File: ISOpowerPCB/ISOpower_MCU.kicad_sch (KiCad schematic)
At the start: 28 parts, among them J2 Conn_01x05_Male, J3 Conn_01x04_Male, J4 Conn_01x06_Male, J5 Conn_01x10_Male, J6 PCB_PIN_header_male, J7 i2c Header, J8 AVR-ISP-6, SW1 SW_Push, U1 ESP32-WROOM-32, U2 IFX27001TFV33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

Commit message: adding logic for fault indication
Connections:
- net GND1 is gone; now on net GND: L1.2
- net GND: now also U1.15 (GND), U1.38 (GND), U1.39 (GND)
- no-connect marks 0 -> 3
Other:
- note added: "This needs to be held high at a minimum"
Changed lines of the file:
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@@
   (junction (at 204.47 85.09) (diameter 0) (color 0 0 0 0)
   )
+  (junction (at 54.61 182.88) (diameter 0) (color 0 0 0 0)
+  )
+  (junction (at 57.15 182.88) (diameter 0) (color 0 0 0 0)
+  )
   (junction (at 49.53 35.56) (diameter 0) (color 0 0 0 0)
   )
@@
   (junction (at 129.54 172.72) (diameter 0) (color 0 0 0 0)
   )
+  (no_connect (at 154.94 63.5))
+  (no_connect (at 199.39 80.01))
+  (no_connect (at 209.55 80.01))
   (wire (pts (xy 185.42 106.68) (xy 254 106.68))
     (stroke (width 0) (type default) (color 0 0 0 0))
@@
     (stroke (width 0) (type default) (color 0 0 0 0))
   )
+  (wire (pts (xy 54.61 182.88) (xy 52.07 182.88))
+    (stroke (width 0) (type default) (color 0 0 0 0))
+  )
   (wire (pts (xy 228.6 31.75) (xy 228.6 34.29))
     (stroke (width 0) (type default) (color 0 0 0 0))
@@
     (stroke (width 0) (type default) (color 0 0 0 0))
   )
+  (wire (pts (xy 137.16 133.35) (xy 143.51 133.35))
+    (stroke (width 0) (type default) (color 0 0 0 0))
+  )
   (wire (pts (xy 143.51 172.72) (xy 148.59 172.72))
     (stroke (width 0) (type default) (color 0 0 0 0))
@@
     (stroke (width 0) (type default) (color 0 0 0 0))
   )
+  (wire (pts (xy 57.15 182.88) (xy 59.69 182.88))
+    (stroke (width 0) (type default) (color 0 0 0 0))
+  )
   (wire (pts (xy 26.67 191.77) (xy 31.75 191.77))
     (stroke (width 0) (type default) (color 0 0 0 0))
@@
     (stroke (width 0) (type default) (color 0 0 0 0))
   )
+  (wire (pts (xy 54.61 182.88) (xy 54.61 180.34))
+    (stroke (width 0) (type default) (color 0 0 0 0))
+  )
   (wire (pts (xy 78.74 151.13) (xy 88.9 151.13))
     (stroke (width 0) (type default) (color 0 0 0 0))
@@
     (stroke (width 0) (type default) (color 0 0 0 0))
   )
+  (wire (pts (xy 143.51 99.06) (xy 143.51 133.35))
+    (stroke (width 0) (type default) (color 0 0 0 0))
+  )
   (wire (pts (xy 185.42 73.66) (xy 194.31 73.66))
     (stroke (width 0) (type default) (color 0 0 0 0))
@@
     (stroke (width 0) (type default) (color 0 0 0 0))
   )
+  (wire (pts (xy 52.07 182.88) (xy 52.07 180.34))
+    (stroke (width 0) (type default) (color 0 0 0 0))
+  )
   (wire (pts (xy 193.04 127) (xy 193.04 124.46))
     (stroke (width 0) (type default) (color 0 0 0 0))
@@
     (stroke (width 0) (type default) (color 0 0 0 0))
   )
+  (wire (pts (xy 57.15 182.88) (xy 54.61 182.88))
+    (stroke (width 0) (type default) (color 0 0 0 0))
+  )
   (wire (pts (xy 49.53 25.4) (xy 49.53 26.67))
     (stroke (width 0) (type default) (color 0 0 0 0))
@@
     (stroke (width 0) (type default) (color 0 0 0 0))
   )
+  (wire (pts (xy 59.69 182.88) (xy 59.69 180.34))
+    (stroke (width 0) (type default) (color 0 0 0 0))
+  )
   (wire (pts (xy 48.26 63.5) (xy 48.26 67.31))
     (stroke (width 0) (type default) (color 0 0 0 0))
   )
-  (wire (pts (xy 57.15 180.34) (xy 57.15 185.42))
+  (wire (pts (xy 57.15 180.34) (xy 57.15 182.88))
     (stroke (width 0) (type default) (color 0 0 0 0))
   )
@@
   )
   (wire (pts (xy 86.36 143.51) (xy 86.36 139.7))
+    (stroke (width 0) (type default) (color 0 0 0 0))
+  )
+  (wire (pts (xy 57.15 182.88) (xy 57.15 185.42))
     (stroke (width 0) (type default) (color 0 0 0 0))
   )
@@
   (text "3V3 Source" (at 29.21 59.69 0)
     (effects (font (size 2.5 2.5)) (justify left bottom))
+  )
+  (text "This needs to be held high \nat a minimum\n" (at 130.81 97.79 0)
+    (effects (font (size 1.27 1.27)) (justify left bottom))
   )
   (text "Current Sensing Bus A" (at 128.27 68.58 0)
@@
   (global_label "MCU_5V_BUS" (shape input) (at 170.18 31.75 90) (fields_autoplaced)
     (effects (font (size 1.27 1.27)) (justify left))
-    (property "Intersheet References" "${INTERSHEET_REFS}" (id 0) (at 170.2594 17.2417 90)
+    (property "Intersheet References" "${INTERSHEET_REFS}" (id 0) (at 170.1006 17.2417 90)
       (effects (font (size 1.27 1.27)) (justify left) hide)
     )
@@
   (global_label "MCU_5V_BUS" (shape output) (at 90.17 29.21 180) (fields_autoplaced)
     (effects (font (size 1.27 1.27)) (justify right))
-    (property "Intersheet References" "${INTERSHEET_REFS}" (id 0) (at 75.6617 29.2894 0)
+    (property "Intersheet References" "${INTERSHEET_REFS}" (id 0) (at 75.6617 29.1306 0)
       (effects (font (size 1.27 1.27)) (justify right) hide)
     )
@@
     )
     (property "Datasheet" "" (id 3) (at 57.15 35.56 0)
-      (effects (font (size 1.27 1.27)) hide)
-    )
-    (pin "1")
-  )
-  (symbol (lib_id "power:GND1") (at 176.53 54.61 0) (unit 1)
-    (in_bom yes) (on_board yes) (fields_autoplaced)
-    (property "Reference" "#PWR022" (id 0) (at 176.53 60.96 0)
-      (effects (font (size 1.27 1.27)) hide)
-    )
-    (property "Value" "GND1" (id 1) (at 179.07 55.8799 0)
-      (effects (font (size 1.27 1.27)) (justify left))
-    )
-    (property "Footprint" "" (id 2) (at 176.53 54.61 0)
-      (effects (font (size 1.27 1.27)) hide)
-    )
-    (property "Datasheet" "" (id 3) (at 176.53 54.61 0)
       (effects (font (size 1.27 1.27)) hide)
     )
@@
     (pin "2")
   )
+  (symbol (lib_id "power:GND") (at 176.53 54.61 0) (unit 1)
+    (in_bom yes) (on_board yes) (fields_autoplaced)
+    (property "Reference" "#PWR022" (id 0) (at 176.53 60.96 0)
+      (effects (font (size 1.27 1.27)) hide)
+    )
+    (property "Value" "GND" (id 1) (at 179.07 55.8799 0)
+      (effects (font (size 1.27 1.27)) (justify left))
+    )
+    (property "Footprint" "" (id 2) (at 176.53 54.61 0)
+      (effects (font (size 1.27 1.27)) hide)
+    )
+    (property "Datasheet" "" (id 3) (at 176.53 54.61 0)
+      (effects (font (size 1.27 1.27)) hide)
+    )
+    (pin "1")
+  )
   (symbol (lib_id "power:GND") (at 130.81 143.51 0) (unit 1)

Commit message: fixed most electrical rules check violations
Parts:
- C1, C2, C3, C4, C5, C6, C7, C8: symbol 000_Capacitor_FIlm_Immo:cap_film_0805 -> 000_Capacitor_Film_Immo:cap_film_0805
- L1: value L -> 10uH
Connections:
- net GND: now also C6.1
- net MCU_5V_BUS: now also C6.2, L1.1, U3.18 (AVCC); no longer C6.1
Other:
- note added: "Big Q About this section here, should AVCC be tied directly to VCC?"
- note added: "Cant see this inductor on schem though"
- note added: "Changing to match arduino provided schematics"
- moved on the sheet: C3, C4

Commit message: Footprint Associations 50% complete
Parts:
- C3, C4, C6: value 100N -> 100n
- D2: value LED_0805_smd -> Blue; footprint Diode_SMD:D_0805_2012Metric_Pad1.15x1.40mm_HandSolder -> LED_SMD:LED_0805_2012Metric_Pad1.15x1.40mm_HandSolder
- J2: footprint (none) -> Connector_PinHeader_1.27mm:PinHeader_1x05_P1.27mm_Vertical
- J3: footprint (none) -> Connector_PinHeader_1.27mm:PinHeader_1x04_P1.27mm_Horizontal
- J4: footprint (none) -> Connector_PinHeader_1.27mm:PinHeader_1x06_P1.27mm_Vertical
- J5: footprint (none) -> Connector_PinHeader_1.27mm:PinHeader_1x10_P1.27mm_Vertical
- J6: value PCB_PIN_header_male -> Conn_01x03_Male; footprint (none) -> Connector_PinHeader_1.27mm:PinHeader_1x03_P1.27mm_Vertical
- J7, J8: footprint (none) -> Connector_PinHeader_1.27mm:PinHeader_2x03_P1.27mm_Vertical
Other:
- sheet Logic Level Conversion ports: added none; removed OE
- note removed: "This needs to be held high at a minimum"
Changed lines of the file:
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@@
-    (stroke (width 0) (type default) (color 0 0 0 0))
-  )
-  (wire (pts (xy 137.16 133.35) (xy 143.51 133.35))
     (stroke (width 0) (type default) (color 0 0 0 0))
   )
@@
   )
   (wire (pts (xy 106.68 29.21) (xy 107.95 29.21))
-    (stroke (width 0) (type default) (color 0 0 0 0))
-  )
-  (wire (pts (xy 143.51 99.06) (xy 143.51 133.35))
     (stroke (width 0) (type default) (color 0 0 0 0))
   )
@@
   (text "3V3 Source" (at 29.21 59.69 0)
     (effects (font (size 2.5 2.5)) (justify left bottom))
-  )
-  (text "This needs to be held high \nat a minimum\n" (at 130.81 97.79 0)
-    (effects (font (size 1.27 1.27)) (justify left bottom))
   )
   (text "Current Sensing Bus A" (at 128.27 68.58 0)
@@
     (in_bom yes) (on_board yes)
     (property "Reference" "C6" (id 0) (at 177.8 35.56 0))
-    (property "Value" "100N" (id 1) (at 179.07 40.64 0))
+    (property "Value" "100n" (id 1) (at 179.07 40.64 0))
     (property "Footprint" "Capacitor_SMD:C_0805_2012Metric_Pad1.18x1.45mm_HandSolder" (id 2) (at 177.8 48.26 0)
       (effects (font (size 1.27 1.27)) hide)
@@
       (effects (font (size 1.27 1.27)) (justify right))
     )
-    (property "Value" "PCB_PIN_header_male" (id 1) (at 127 30.4799 0)
+    (property "Value" "Conn_01x03_Male" (id 1) (at 127 30.4799 0)
       (effects (font (size 1.27 1.27)) (justify right))
     )
-    (property "Footprint" "" (id 2) (at 125.73 29.21 0)
+    (property "Footprint" "Connector_PinHeader_1.27mm:PinHeader_1x03_P1.27mm_Vertical" (id 2) (at 125.73 29.21 0)
       (effects (font (size 1.27 1.27)) hide)
     )
@@
     (in_bom yes) (on_board yes)
     (property "Reference" "C4" (id 0) (at 35.56 38.1 0))
-    (property "Value" "100N" (id 1) (at 36.83 43.18 0))
+    (property "Value" "100n" (id 1) (at 36.83 43.18 0))
     (property "Footprint" "Capacitor_SMD:C_0805_2012Metric_Pad1.18x1.45mm_HandSolder" (id 2) (at 35.56 50.8 0)
       (effects (font (size 1.27 1.27)) hide)
@@
     (property "Reference" "J4" (id 0) (at 27.305 139.7 0))
     (property "Value" "Conn_01x06_Male" (id 1) (at 27.305 142.24 0))
-    (property "Footprint" "" (id 2) (at 26.67 149.86 0)
+    (property "Footprint" "Connector_PinHeader_1.27mm:PinHeader_1x06_P1.27mm_Vertical" (id 2) (at 26.67 149.86 0)
       (effects (font (size 1.27 1.27)) hide)
     )
@@
       (effects (font (size 1.27 1.27)) (justify right))
     )
-    (property "Footprint" "" (id 2) (at 93.98 161.29 0)
+    (property "Footprint" "Connector_PinHeader_1.27mm:PinHeader_1x10_P1.27mm_Vertical" (id 2) (at 93.98 161.29 0)
       (effects (font (size 1.27 1.27)) hide)
     )
@@
     (property "Reference" "J2" (id 0) (at 22.225 176.53 0))
     (property "Value" "Conn_01x05_Male" (id 1) (at 22.225 179.07 0))
-    (property "Footprint" "" (id 2) (at 21.59 186.69 0)
+    (property "Footprint" "Connector_PinHeader_1.27mm:PinHeader_1x05_P1.27mm_Vertical" (id 2) (at 21.59 186.69 0)
       (effects (font (size 1.27 1.27)) hide)
     )
@@
       (effects (font (size 1.27 1.27)) (justify right))
     )
-    (property "Footprint" "" (id 2) (at 163.83 177.8 0)
+    (property "Footprint" "Connector_PinHeader_1.27mm:PinHeader_2x03_P1.27mm_Vertical" (id 2) (at 163.83 177.8 0)
       (effects (font (size 1.27 1.27)) hide)
     )
@@
       (effects (font (size 1.27 1.27)) (justify right))
     )
-    (property "Footprint" "" (id 2) (at 232.41 45.72 90)
+    (property "Footprint" "Connector_PinHeader_1.27mm:PinHeader_2x03_P1.27mm_Vertical" (id 2) (at 232.41 45.72 90)
       (effects (font (size 1.27 1.27)) hide)
     )
@@
     (property "Reference" "J3" (id 0) (at 27.305 114.3 0))
     (property "Value" "Conn_01x04_Male" (id 1) (at 27.305 116.84 0))
-    (property "Footprint" "" (id 2) (at 26.67 121.92 0)
+    (property "Footprint" "Connector_PinHeader_1.27mm:PinHeader_1x04_P1.27mm_Horizontal" (id 2) (at 26.67 121.92 0)
       (effects (font (size 1.27 1.27)) hide)
     )
@@
     (in_bom yes) (on_board yes)
     (property "Reference" "C3" (id 0) (at 35.56 27.94 0))
-    (property "Value" "100N" (id 1) (at 36.83 33.02 0))
+    (property "Value" "100n" (id 1) (at 36.83 33.02 0))
     (property "Footprint" "Capacitor_SMD:C_0805_2012Metric_Pad1.18x1.45mm_HandSolder" (id 2) (at 35.56 40.64 0)
       (effects (font (size 1.27 1.27)) hide)
@@
       (effects (font (size 1.27 1.27)) (justify right))
     )
-    (property "Value" "LED_0805_smd" (id 1) (at 196.85 133.6674 90)
+    (property "Value" "Blue" (id 1) (at 196.85 133.6674 90)
       (effects (font (size 1.27 1.27)) (justify right))
     )
-    (property "Footprint" "Diode_SMD:D_0805_2012Metric_Pad1.15x1.40mm_HandSolder" (id 2) (at 200.66 129.54 0)
+    (property "Footprint" "LED_SMD:LED_0805_2012Metric_Pad1.15x1.40mm_HandSolder" (id 2) (at 200.66 129.54 0)
       (effects (font (size 1.27 1.27)) hide)
     )
@@
       (effects (font (size 1.27 1.27)) (justify right))
     )
-    (pin "OE" input (at 137.16 133.35 0)
-      (effects (font (size 1.27 1.27)) (justify right))
-    )

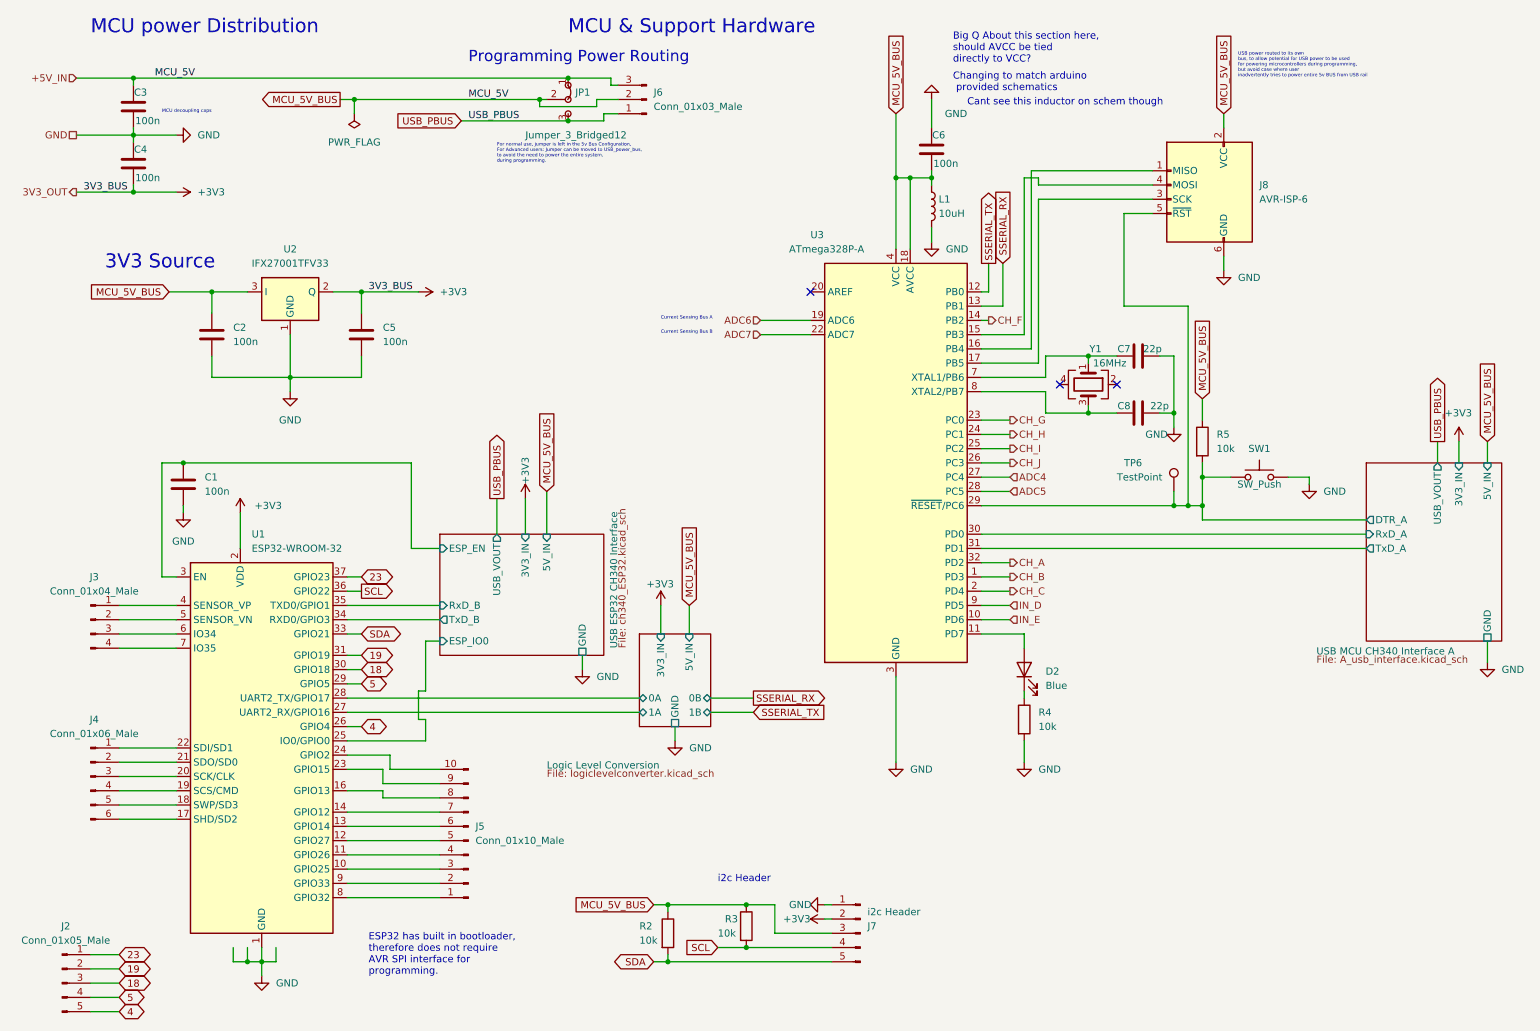
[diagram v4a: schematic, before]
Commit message: added documentation for component selection
Completed footprint association & added documentation re Netclasses. Need to update netclasses in schematic settings before moving to PCB layout.
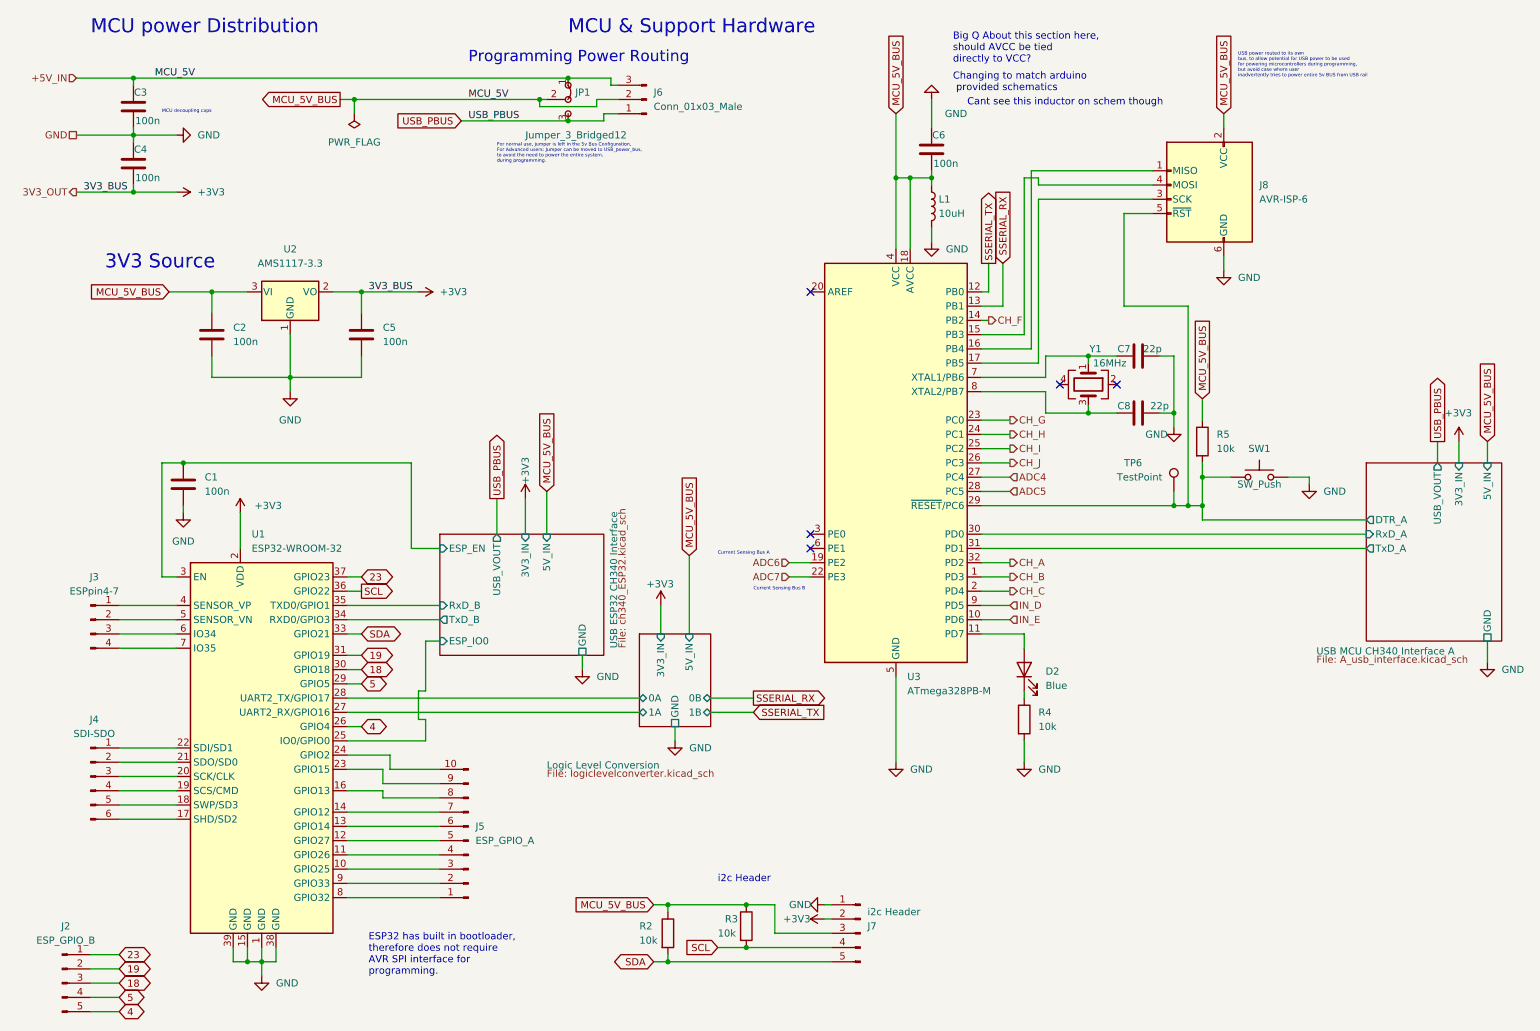
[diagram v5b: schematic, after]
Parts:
- removed U2: IFX27001TFV33, Package_TO_SOT_SMD:TO-252-3_TabPin2, symbol Regulator_Linear:IFX27001TFV33
- removed U3: ATmega328P-A, Package_QFP:TQFP-32_7x7mm_P0.8mm, symbol MCU_Microchip_ATmega:ATmega328P-A
- added U2: AMS1117-3.3, Package_TO_SOT_SMD:TO-252-3_TabPin2, symbol Regulator_Linear:AMS1117-3.3
- added U3: ATmega328PB-M, Package_DFN_QFN:QFN-32-1EP_5x5mm_P0.5mm_EP3.1x3.1mm, symbol MCU_Microchip_ATmega:ATmega328PB-M
- J2: value Conn_01x05_Male -> ESP_GPIO_B
- J3: value Conn_01x04_Male -> ESPpin4-7; footprint Connector_PinHeader_1.27mm:PinHeader_1x04_P1.27mm_Horizontal -> Connector_PinHeader_1.27mm:PinHeader_1x04_P1.27mm_Vertical
- J4: value Conn_01x06_Male -> SDI-SDO
- J5: value Conn_01x10_Male -> ESP_GPIO_A
- JP1: footprint (none) -> Jumper:SolderJumper-3_P1.3mm_Bridged12_RoundedPad1.0x1.5mm_NumberLabels
- L1: footprint (none) -> Inductor_SMD:L_0805_2012Metric_Pad1.05x1.20mm_HandSolder
- SW1: footprint (none) -> Button_Switch_SMD:SW_SPST_EVQPE1
- TP6: footprint (none) -> TestPoint:TestPoint_Pad_D1.5mm
- Y1: footprint (none) -> Crystal:Crystal_SMD_Abracon_ABM3C-4Pin_5.0x3.2mm
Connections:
- net +3V3: now also U2.2 (VO)
- net ADC4: now also U3.27 (PC4)
- net ADC5: now also U3.28 (PC5)
- net ADC6: now also U3.19 (PE2)
- net ADC7: now also U3.22 (PE3)
- net CH_A: now also U3.32 (PD2)
- net CH_B: now also U3.1 (PD3)
- net CH_C: now also U3.2 (PD4)
- net CH_F: now also U3.14 (PB2)
- net CH_G: now also U3.23 (PC0)
- net CH_H: now also U3.24 (PC1)
- net CH_I: now also U3.25 (PC2)
- net CH_J: now also U3.26 (PC3)
- net GND: now also U2.1 (GND), U3.21 (GND), U3.33 (GND), U3.5 (GND)
- net IN_D: now also U3.9 (PD5)
- net IN_E: now also U3.10 (PD6)
- net MCU_5V_BUS: now also U2.3 (VI), U3.18 (AVCC), U3.4 (VCC)
- net SSERIAL_RX: now also U3.13 (PB1)
- net SSERIAL_TX: now also U3.12 (PB0)
- net USB MCU CH340 Interface A/DTR_A: now also U3.29 (~{RESET}/PC6)
- net USB MCU CH340 Interface A/RxD_A: now also U3.30 (PD0)
- net USB MCU CH340 Interface A/TxD_A: now also U3.31 (PD1)
- net at C7.1, Y1.1: now also U3.7 (XTAL1/PB6)
- net at C8.1, Y1.3: now also U3.8 (XTAL2/PB7)
- net at J8.1 (MISO): now also U3.16 (PB4)
- net at J8.3 (SCK): now also U3.17 (PB5)
- net at J8.4 (MOSI): now also U3.15 (PB3)
- net at D2.2 (A): now also U3.11 (PD7)
- no-connect marks 3 -> 5

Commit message: added netclasses
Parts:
- J6: value Conn_01x03_Male -> prog_power_select
- JP1: value Jumper_3_Bridged12 -> prog_power_select
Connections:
- net MCU_5V_BUS: no longer C3.1, J6.3 (Pin_3), JP1.1 (A)
- new net +5V_IN: C3.1, J6.3 (Pin_3), JP1.1 (A)
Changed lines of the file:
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@@
     (effects (font (size 1.27 1.27)) (justify left bottom))
   )
-  (label "3V3_BUS" (at 76.2 63.5 0)
-    (effects (font (size 1.27 1.27)) (justify left bottom))
-  )
-  (label "MCU_5V" (at 38.1 25.4 0)
+  (label "MCU_5V_BUS" (at 80.01 29.21 0)
     (effects (font (size 1.27 1.27)) (justify left bottom))
   )
@@
   )
   (label "3V3_BUS" (at 25.4 45.72 0)
-    (effects (font (size 1.27 1.27)) (justify left bottom))
-  )
-  (label "MCU_5V" (at 93.98 29.21 0)
     (effects (font (size 1.27 1.27)) (justify left bottom))
   )
@@
       (effects (font (size 1.27 1.27)) (justify right))
     )
-    (property "Value" "Conn_01x03_Male" (id 1) (at 127 30.4799 0)
+    (property "Value" "prog_power_select" (id 1) (at 127 30.4799 0)
       (effects (font (size 1.27 1.27)) (justify right))
     )
@@
       (effects (font (size 1.27 1.27)) (justify left))
     )
-    (property "Value" "Jumper_3_Bridged12" (id 1) (at 104.14 35.56 90)
-      (effects (font (size 1.27 1.27)) (justify left))
-    )
+    (property "Value" "prog_power_select" (id 1) (at 104.14 35.56 90)
+      (effects (font (size 1.27 1.27)) (justify left))
+    )
